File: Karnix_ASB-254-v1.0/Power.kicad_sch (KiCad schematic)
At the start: 37 parts, among them U1 ST1S14, U2 TLV62565DBVT, U3 RS3236-2.5YF5, U3 RS3236-3.3YF5

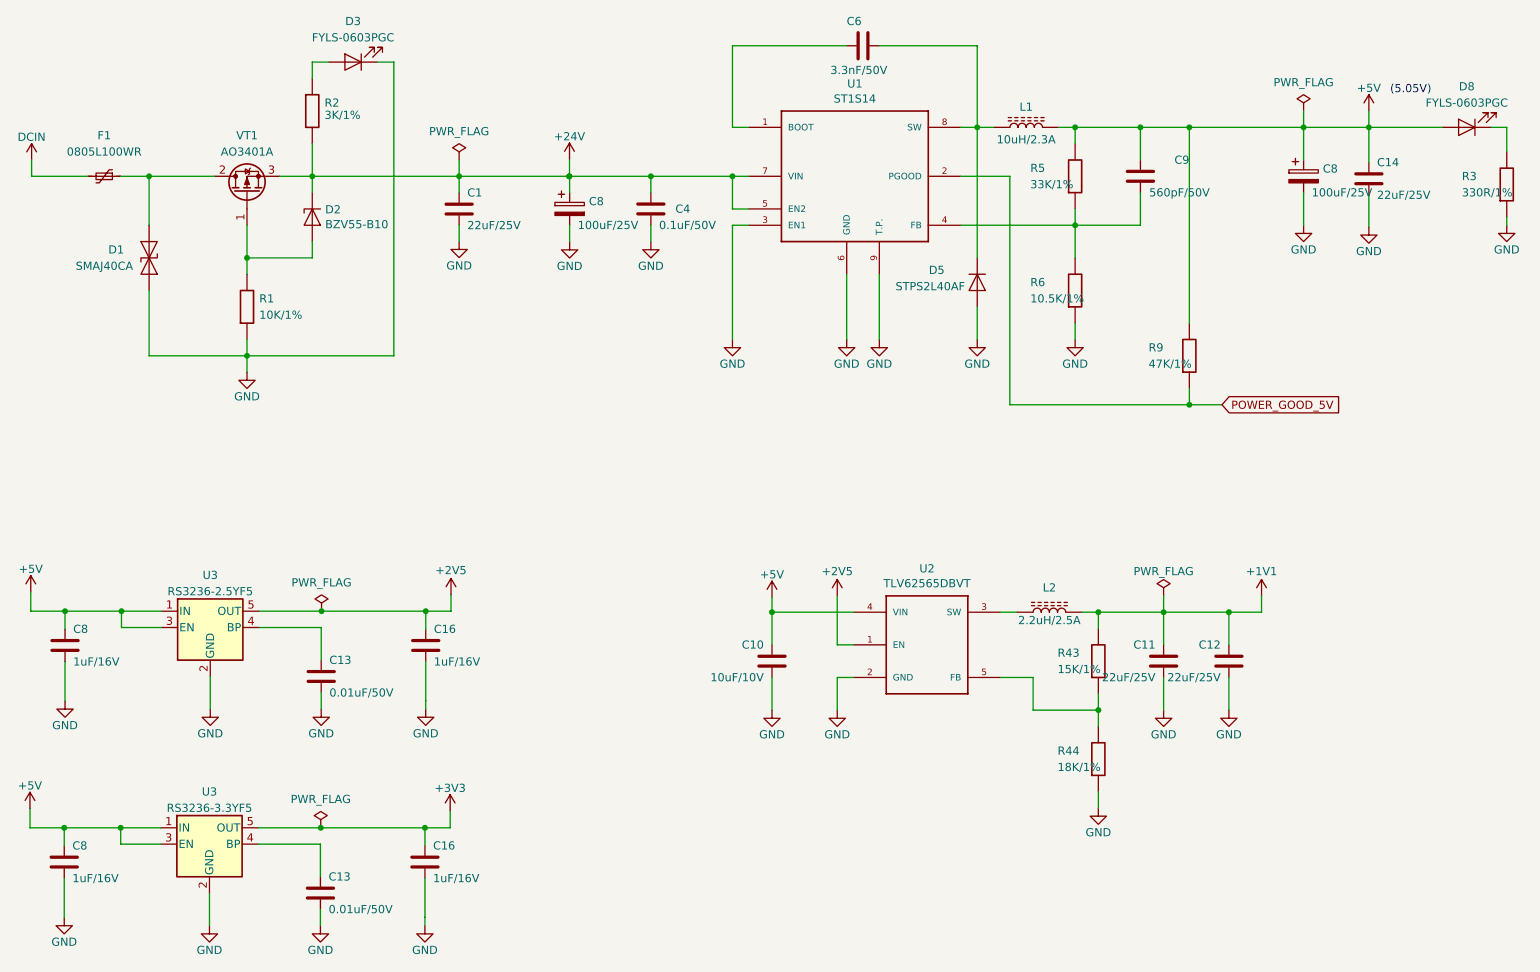
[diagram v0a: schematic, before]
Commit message: Remove rudimentary referencies to old projects
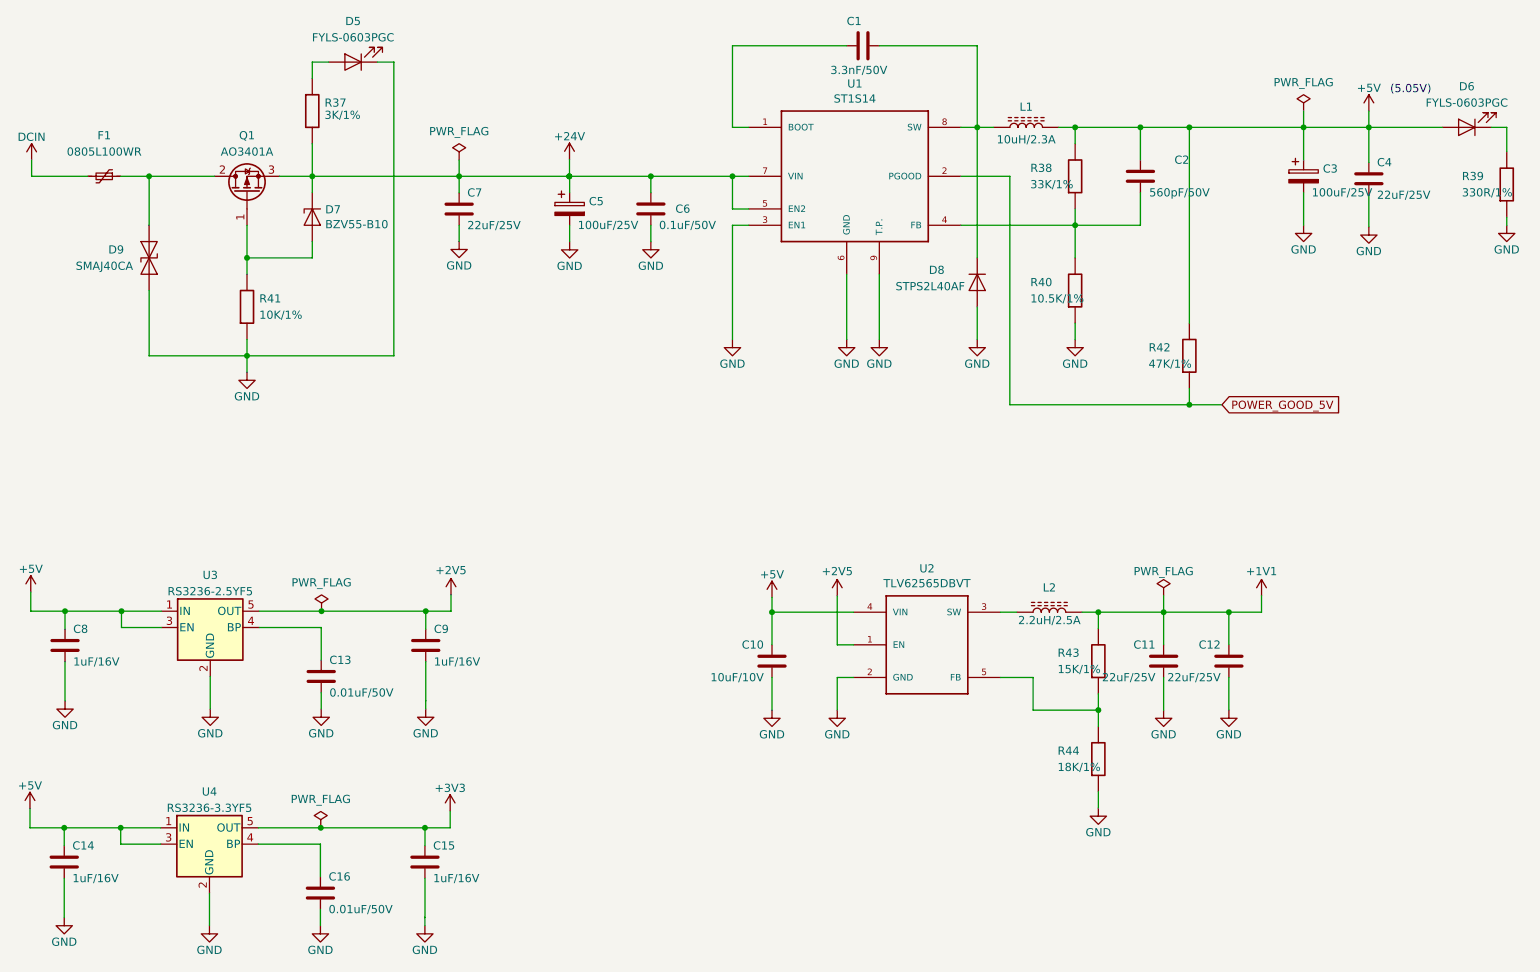
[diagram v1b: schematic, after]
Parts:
- renumbered C6 to C1, C8 to C14, C16 to C15, C13 to C16, C9 to C2, C8 to C3, C14 to C4, C8 to C5, C4 to C6, C1 to C7, C16 to C9, D3 to D5, D8 to D6, D2 to D7, D5 to D8, D1 to D9, VT1 to Q1, R2 to R37, R5 to R38, R3 to R39, R6 to R40, R1 to R41, R9 to R42, U3 to U4
